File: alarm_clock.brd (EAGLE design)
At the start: 100 x 80 mm, 33 parts, among them Q1 16MHz, U1 ATMEGA328P-PU, U2 MC14489BPE, U3 DS3231

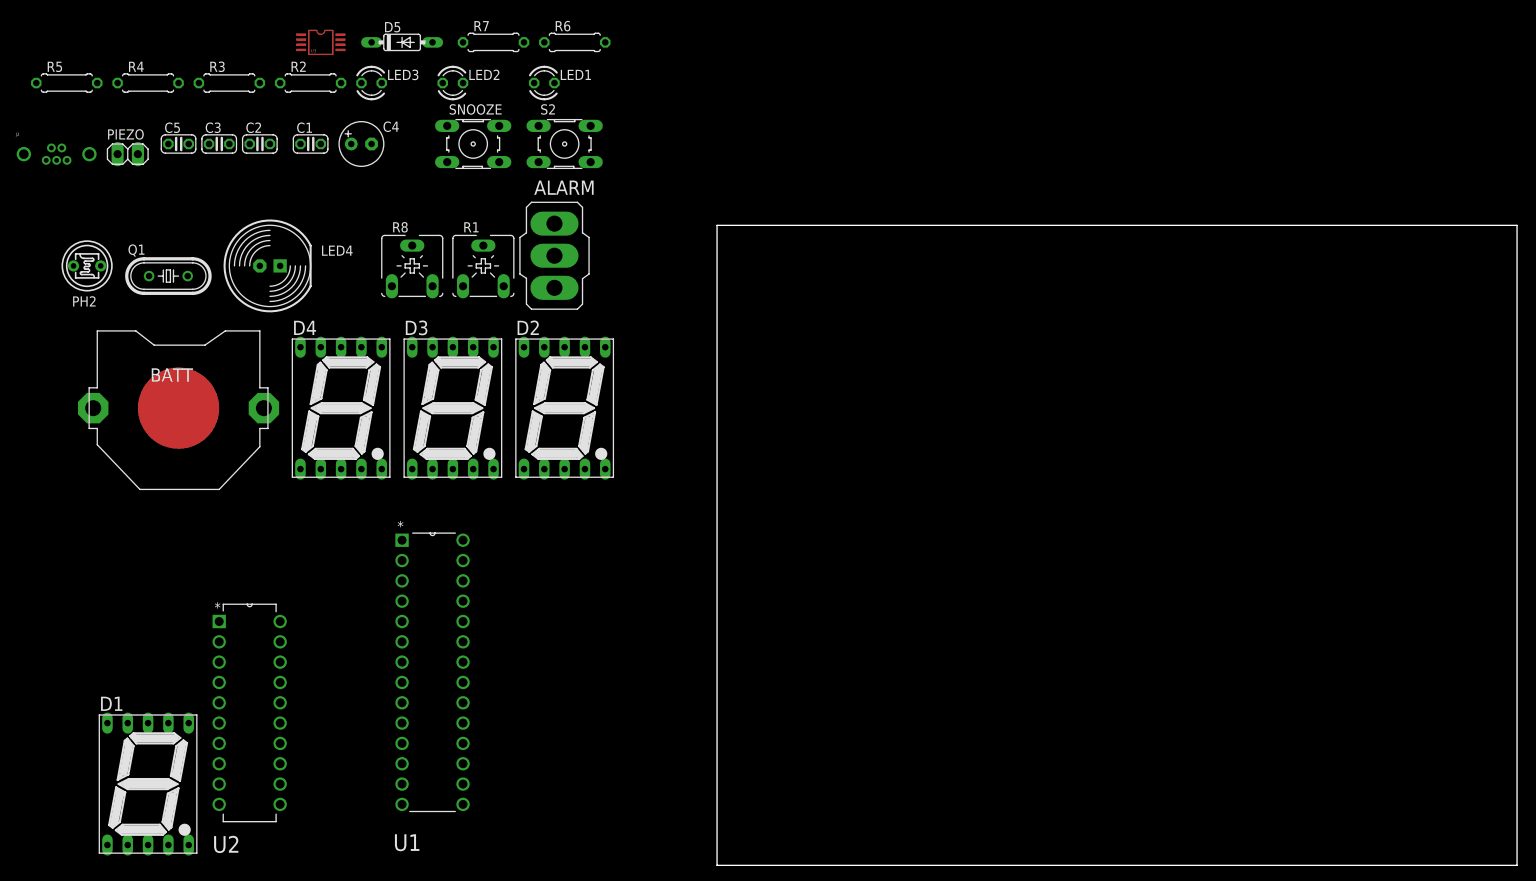
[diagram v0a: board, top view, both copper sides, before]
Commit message: Initial board set-up (no routes):
Initial board set-up (pre route) with toggle switch on pcb and pin connectors
shown on reverse side of board.
Schematic amended accordingly.
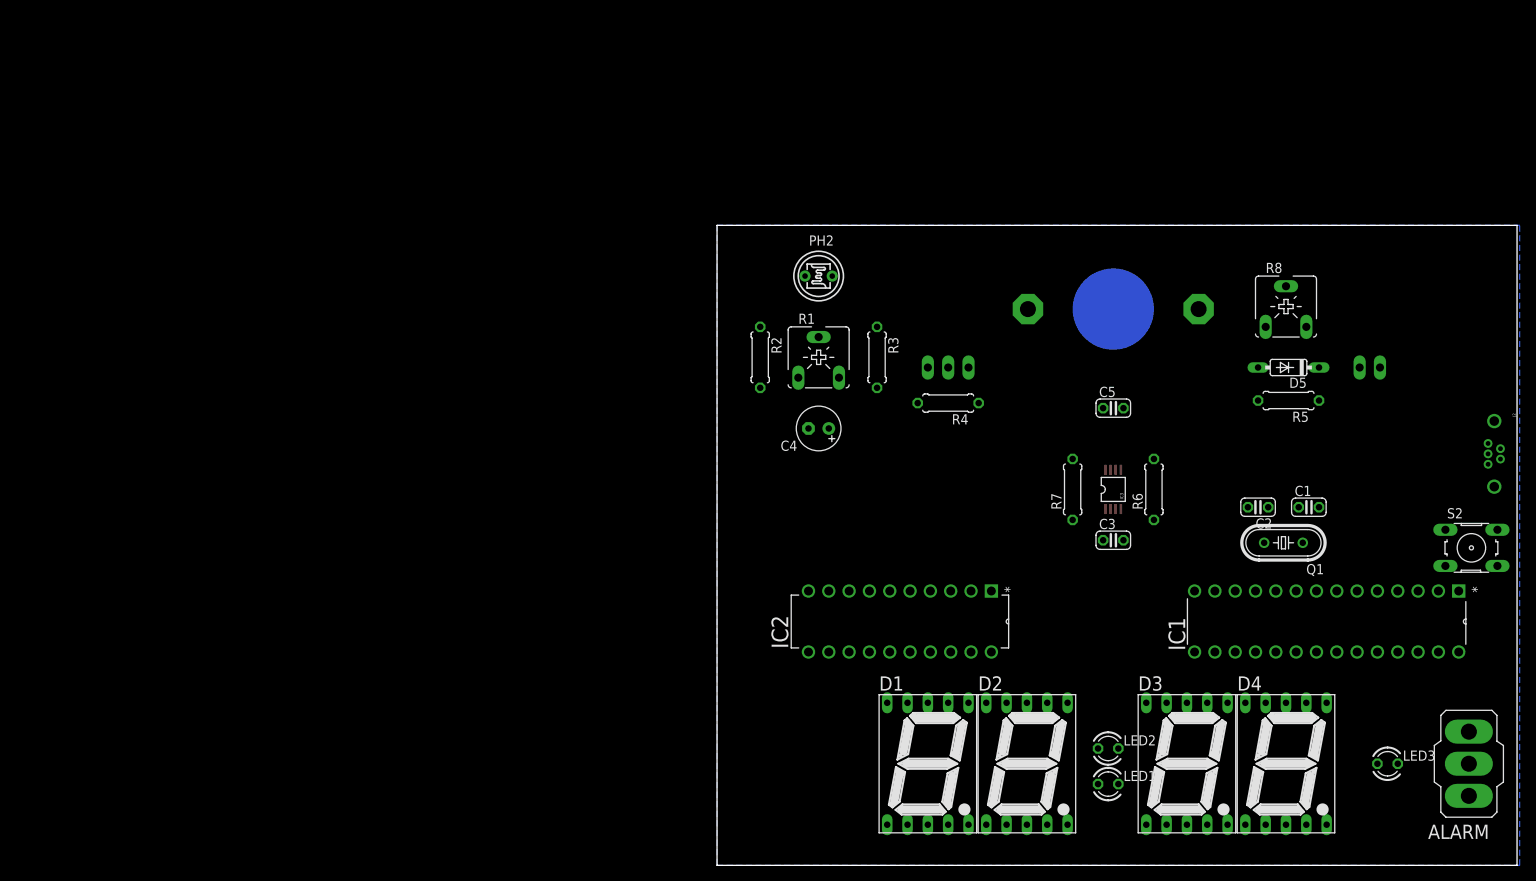
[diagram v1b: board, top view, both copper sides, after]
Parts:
- removed LED4: Snooze, led:LED10MM
- removed U1: ATMEGA328P-PU, Atmel_By_element14_Batch_1-00:DIP254P762X457-28
- removed U2: MC14489BPE, MC14489BPE:DIP254P762X457-20
- removed U3: DS3231, ds3231:DS3231-8_SO
- added IC1: ATMEGA328P-PU, Atmel_By_element14_Batch_1-00:DIP254P762X457-28
- added IC2: MC14489BPE, MC14489BPE:DIP254P762X457-20
- added IC3: DS3231, ds3231:DS3231-8_SO
- ALARM: value (none) -> S1
- PIEZO: device pinhead:1X02 -> pinhead:1X02/90
- SNOOZE: device switch-omron:B3F-10XX -> pinhead:1X03/90
- moved J2 183.6 mm to (97.2, 51.4), turned to 270 degrees
- moved R5 157.8 mm to (71.4, 58.1), turned to 180 degrees
- moved PIEZO 156.9 mm to (81.6, 66.0), flipped to the bottom
- moved LED3 152.9 mm to (83.8, 12.7)
- moved Q1 143.3 mm to (70.8, 40.3), turned to 180 degrees
- moved C1 132.8 mm to (74.0, 44.8)
- moved C2 132.8 mm to (67.6, 44.8), turned to 180 degrees
- moved ALARM 130.8 mm to (94.0, 12.7), turned to 180 degrees
- moved D4 126.2 mm to (71.1, 12.7)
- moved S2 124.1 mm to (94.3, 39.7)
- moved C3 122.2 mm to (49.5, 40.6)
- moved C5 121.4 mm to (49.5, 57.1)
- moved D5 118.0 mm to (71.4, 62.2), turned to 180 degrees
- moved BATT 117.5 mm to (49.5, 69.5), flipped to the bottom
- moved LED2 116.7 mm to (48.9, 14.6)
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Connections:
- removed net N$3: U2.12
- net A: now also IC2.7; no longer U2.7
- net B: now also IC2.6; no longer U2.6
- net C: now also IC2.5; no longer U2.5
- net CLK: now also IC1.13, IC2.11; no longer U1.13, U2.11
- net D: now also IC2.4; no longer U2.4
- net D1: now also IC2.9; no longer U2.9
- net D2: now also IC2.13; no longer U2.13
- net D3: now also IC2.15; no longer U2.15
- net D4: now also IC2.16; no longer U2.16
- net DATA: now also IC1.14, IC2.12; no longer U1.14
- net E: now also IC2.2; no longer U2.2
- net EN: now also IC1.6, IC2.10; no longer U1.6, U2.10
- net F: now also IC2.1; no longer U2.1
- net G: now also IC2.20; no longer U2.20
- net GND: now also IC1.22, IC1.8, IC2.14, IC3.5; no longer LED4.K, SNOOZE.1, U1.22, U1.8, U2.14, U3.P$5
- net LEDS: now also IC2.17; no longer U2.17
- net N$18: now also IC1.10; no longer U1.10
- net N$19: now also IC1.9; no longer U1.9
- net N$2: now also SNOOZE.3; no longer LED4.A
- net N$5: now also IC1.23; no longer U1.23
- net N$6: now also IC1.24; no longer U1.24
- net N$9: now also IC1.25, SNOOZE.1; no longer SNOOZE.3, SNOOZE.4, U1.25
- net P: now also IC2.19; no longer U2.19
- net PZ: now also IC1.5; no longer U1.5
- net RESET: now also IC1.1; no longer U1.1
- net RX: now also IC2.8; no longer U2.8
- net SCL: now also IC1.27, IC3.8; no longer U1.27, U3.P$8
- net SDA: now also IC1.28, IC3.7; no longer U1.28, U3.P$7
- net SNZ: now also IC1.11; no longer U1.11
- net VBAT: now also IC3.6; no longer U3.P$6
- net VCC: now also IC1.20, IC1.7, IC2.3, IC3.2; no longer U1.20, U1.7, U2.3, U3.P$2
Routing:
- added copper zone on layer 16, net GND
